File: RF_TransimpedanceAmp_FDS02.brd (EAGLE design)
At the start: 50.8 x 38.1 mm, 31 parts, among them IC1 PMA-5452, IC3 PMA-5452, IC4 ADM7150ARDZ-3.0, IC5 ADM7150ARDZ-5.0, X1 SMAJ502

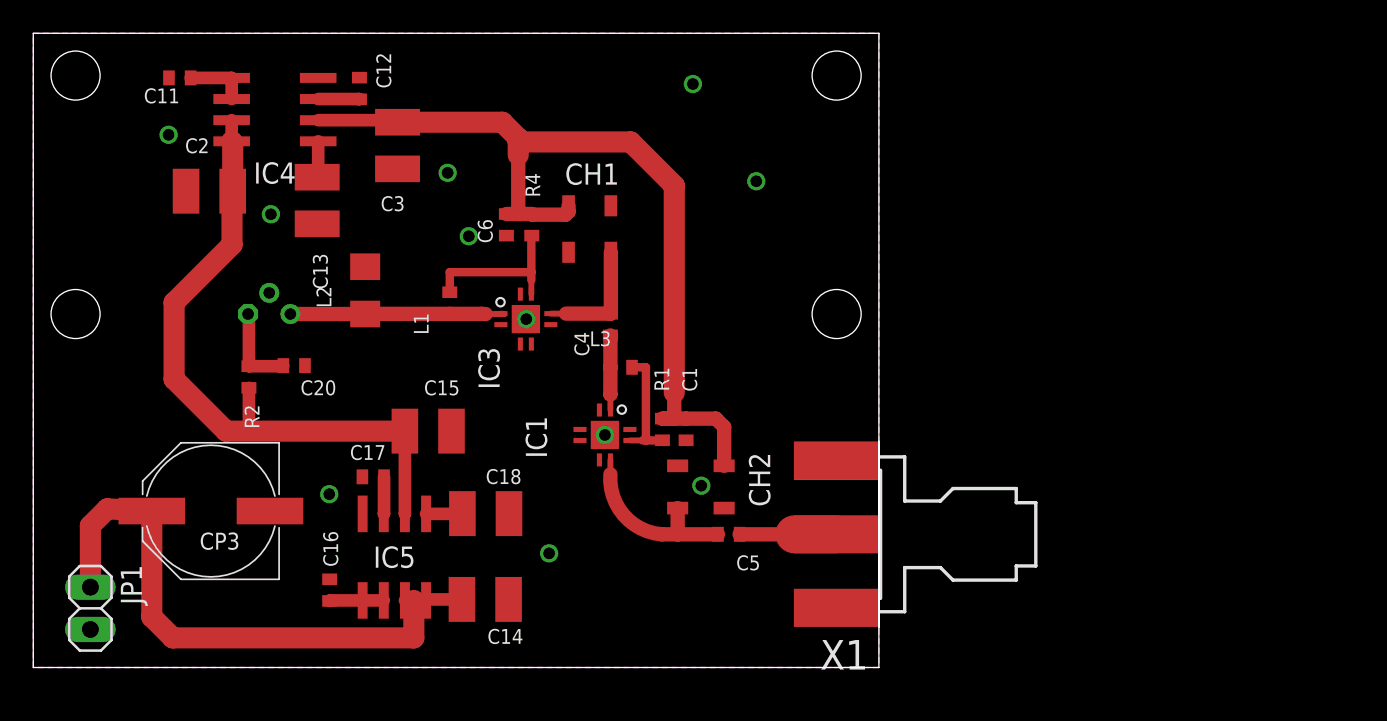
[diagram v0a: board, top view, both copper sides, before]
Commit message: Added third stage amplifier, fixed layout issues.
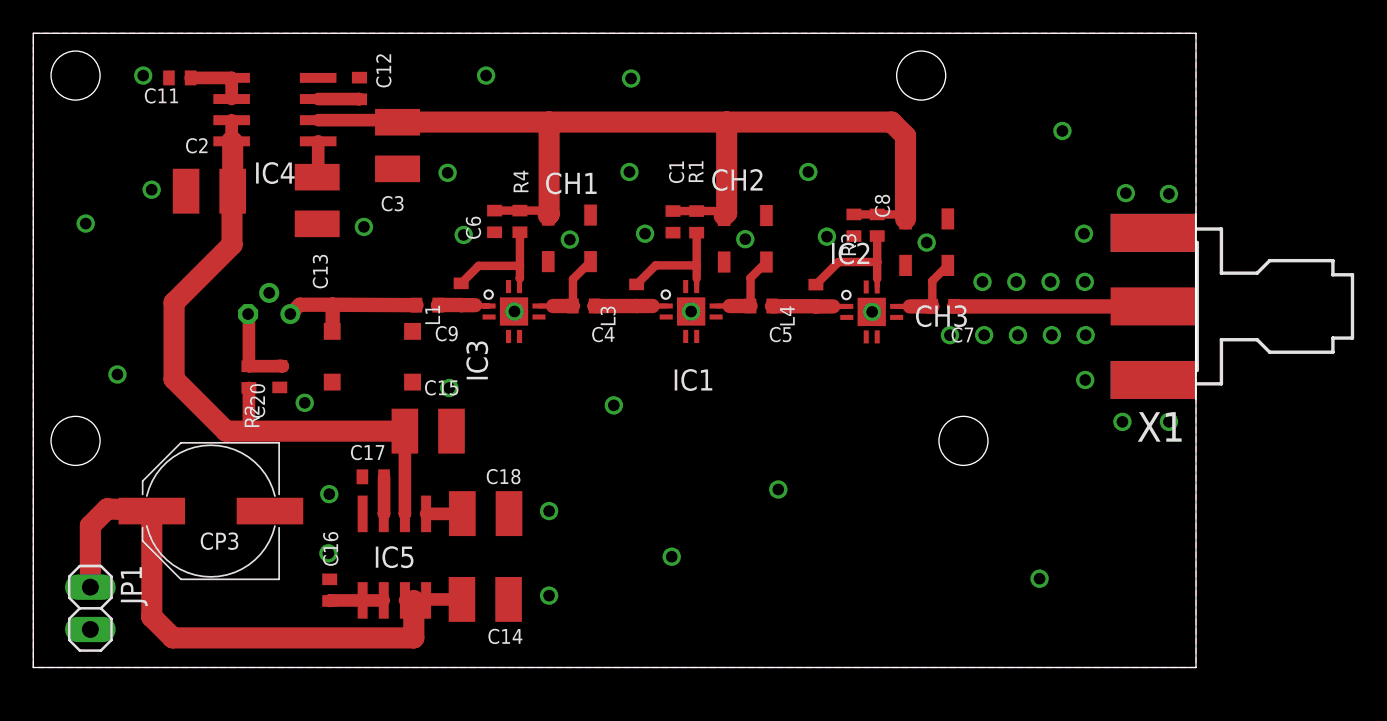
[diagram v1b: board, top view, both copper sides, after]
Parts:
- added C7, C8, C9: 100nF, rlc-jqi:0402
- added CH3: TCCH-80, rf-jqi:GU1604
- added IC2: PMA-5452, rf-jqi:DQ849
- added L4: 390nH, rlc-jqi:0402
- added R3: 1k, rlc-jqi:0402
- L2: value Ferrite Bead -> BCR-802JLB; device rlc-jqi:1206 -> coilcraft-jqi:BCR-MED
- moved X1 23.4 mm to (68.6, 23.0)
- moved CH2 15.1 mm to (42.8, 25.8), turned to 180 degrees
- moved C5 13.9 mm to (43.7, 21.7)
- moved R1 12.6 mm to (39.9, 26.8)
- moved C1 12.5 mm to (38.4, 26.8)
- moved IC1 8.91 mm to (39.5, 20.4), turned to 0 degrees
- moved L3 4.43 mm to (36.2, 22.4), turned to 90 degrees
- moved L2 4.01 mm to (20.4, 18.7), turned to 180 degrees
- moved C4 1.95 mm to (33.1, 21.7), turned to 180 degrees
- moved CH1 1.34 mm to (32.2, 25.8)
- moved C20 1.09 mm to (14.8, 17.5), turned to 90 degrees
- moved L1 0.87 mm to (25.7, 22.4)
- moved IC3 0.85 mm to (28.9, 20.4)
- moved R4 0.74 mm to (29.2, 26.8)
- moved C6 0.74 mm to (27.7, 26.8)
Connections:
- new net N$10: IC2.P$7, L4.2, R3.1
- new net N$4: C7.1, X1.1
- new net N$8: C7.2, CH3.P$1, IC2.P$6
- new net RFPD2: C5.1, IC2.P$1, L4.1
- net +3V: now also C8.1, CH3.P$3, R3.2
- net GND: now also C8.2, IC2.P$GND, L2.2; no longer L2.1
- net N$7: now also C9.2, L2.1, PD1.P$3; no longer C5.1, X1.1
- net RFPD: now also C9.1; no longer L2.2, PD1.P$3
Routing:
- net N$4: track 0.00 -> 11.9 mm
- net RFPD: track 13.1 -> 3.42 mm
- net +3V: track 52.7 -> 61.7 mm
- net N$10: track 0.00 -> 7.30 mm
- net N$2: track 10.6 -> 5.10 mm
- net N$8: track 0.00 -> 4.99 mm
- net RFPD2: track 0.00 -> 4.49 mm
- net N$7: track 5.80 -> 9.42 mm
- net N$9: track 9.65 -> 7.24 mm
- net N$6: track 7.29 -> 5.15 mm
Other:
- board size 50.8 x 38.1 mm -> 69.8 x 38.1 mm
